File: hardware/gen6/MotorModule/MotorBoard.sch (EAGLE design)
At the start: 42 parts, among them J1 M20X2SHROUDED

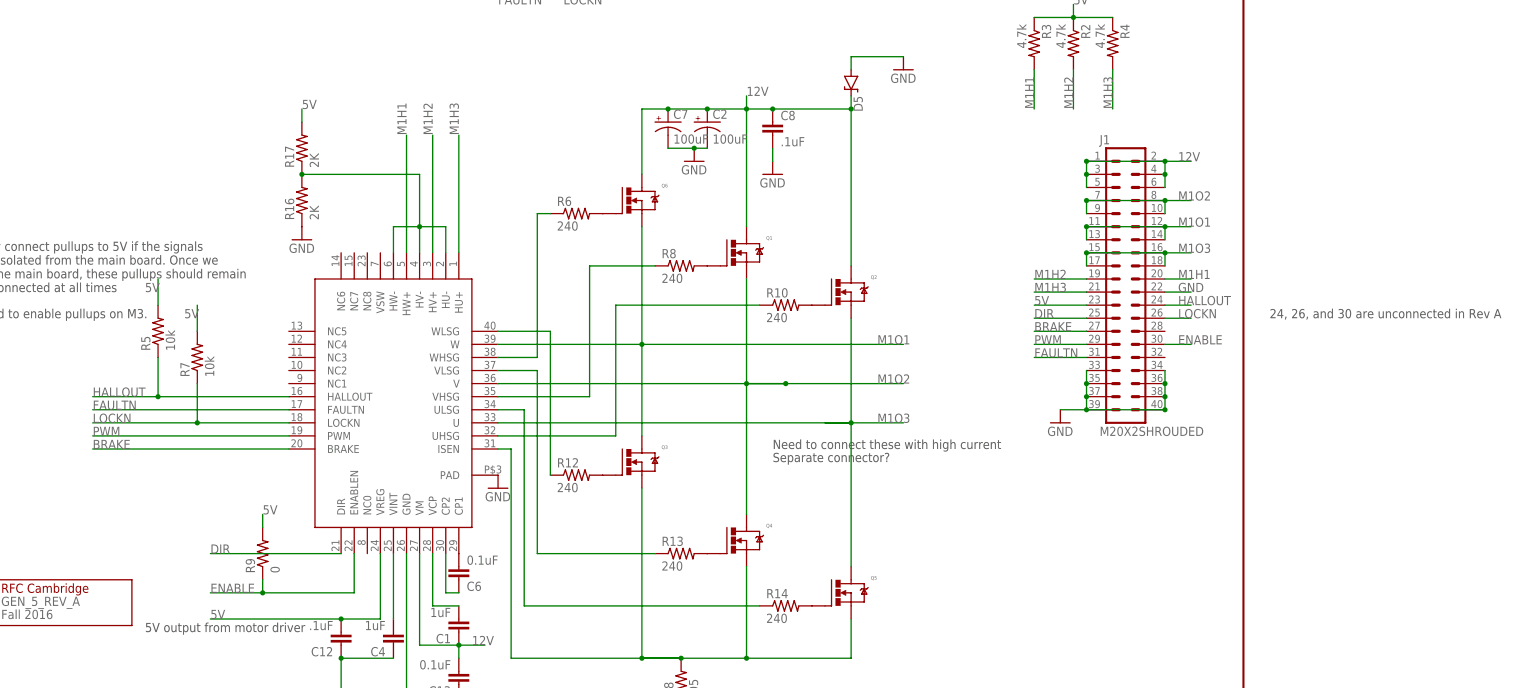
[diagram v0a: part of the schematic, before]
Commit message: new motor controller
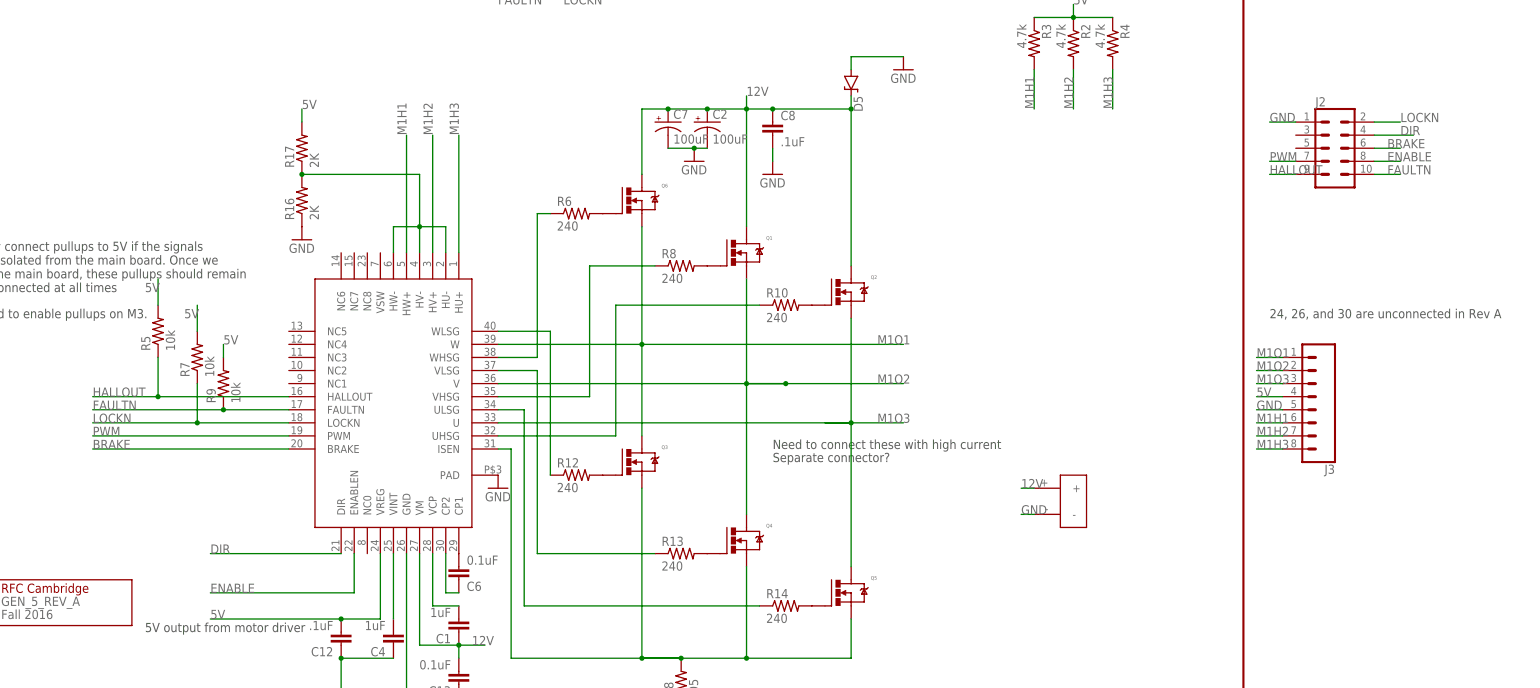
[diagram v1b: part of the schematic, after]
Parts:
- removed J1: M20X2SHROUDED, SparkFun-Connectors:M20X2SHROUDED
- added J2: (no value), SparkFun-Connectors:CONN_05X2SHD
- added J3: (no value), SparkFun-Connectors:CONN_08LONGPADS
- added U$2: POWER_CONN_2X1, Kicker:POWER_CONN_2X1
- R9: value 0 -> 10k
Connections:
- net 12V: now also U$2.+; no longer J1.1, J1.2, J1.3, J1.4, J1.5, J1.6
- net 5V: now also J3.4; no longer J1.23
- net BRAKE: now also J2.6; no longer J1.27
- net DIR: now also J2.4; no longer J1.25
- net ENABLE: now also J2.8; no longer J1.30, R9.1
- net FAULTN: now also J2.10, R9.1; no longer J1.31
- net GND: now also J2.1, J3.5, U$2.-; no longer J1.22, J1.33, J1.34, J1.35, J1.36, J1.37, J1.38, J1.39, J1.40
- net HALLOUT: now also J2.9; no longer J1.24
- net LOCKN: now also J2.2; no longer J1.26
- net M1H1: now also J3.6; no longer J1.20
- net M1H2: now also J3.7; no longer J1.19
- net M1H3: now also J3.8; no longer J1.21
- net M1O1: now also J3.1; no longer J1.11, J1.12, J1.13, J1.14
- net M1O2: now also J3.2; no longer J1.10, J1.7, J1.8, J1.9
- net M1O3: now also J3.3; no longer J1.15, J1.16, J1.17, J1.18
- net PWM: now also J2.7; no longer J1.29
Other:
- moved on the sheet: R9

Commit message: started conversion
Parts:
- added C3, C5: .1uF, SparkFun-Passives:CAP0805
- added IC1: 4011D, 40xx:4011D
- added R11, R25: 4.7k, SparkFun-Resistors:RESISTOR0805-RES
- added R15, R19, R20, R21, R22: 1k, SparkFun-Resistors:RESISTOR0805-RES
- added R23, R24: 10k, SparkFun-Resistors:RESISTOR0805-RES
- added U1: SN74LVC1G32DCKR, SparkFun-IC-Logic:74LVC32DBV
- added U2: 74HC1G04, SparkFun-IC-Logic:74HC1G04
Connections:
- new net N$12: R11.1, R15.1
- new net N$23: R19.2
- new net N$24: R19.1
- new net N$25: U1G1.A, U2G1.A
- new net N$26: IC1A.I1, U2G1.Y
- new net N$27: IC1A.I0, U1G1.B
- new net N$28: U1G1.Y
- new net N$29: R21.2
- new net N$30: R21.1
- new net N$31: IC1A.O
- new net N$32: R20.1
- new net N$33: R20.2
- new net N$34: R22.2, R23.1
- new net N$35: R23.2, R24.1
- new net N$36: R22.1, R24.2
- new net N$37: R25.2
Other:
- note added: "BRK"
- note added: "DIR"
- note added: "INa"
- note added: "INb"

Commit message: finished beginnings of schematic
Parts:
- added C10: 47uF, rcl:CPOL-US085CS-1AW
- added C9: .1uF, SparkFun-Passives:CAP0805
- added LED1, LED2: (no value), led:LED
- added Q7: IRFP250, transistor-power:IRFP250
- C3: value .1uF -> 33nF
- C5: value .1uF -> 47uF; device SparkFun-Passives:CAP0805 -> rcl:CPOL-US085CS-1AW
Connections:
- removed net N$33: R20.2
- new net +5V: Q7.S
- new net N$38: LED1.C, LED2.A, R25.1
- new net N$39: LED1.A, LED2.C
- net GND: now also C10.-, C3.2, C5.-, C9.1, R22.1, R24.2
- net N$35: now also C3.1, R20.2
- net N$36: now also C10.+, C5.+, C9.2, Q7.D; no longer R22.1, R24.2
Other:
- note added: "JP7"
- note added: "check with schematic"

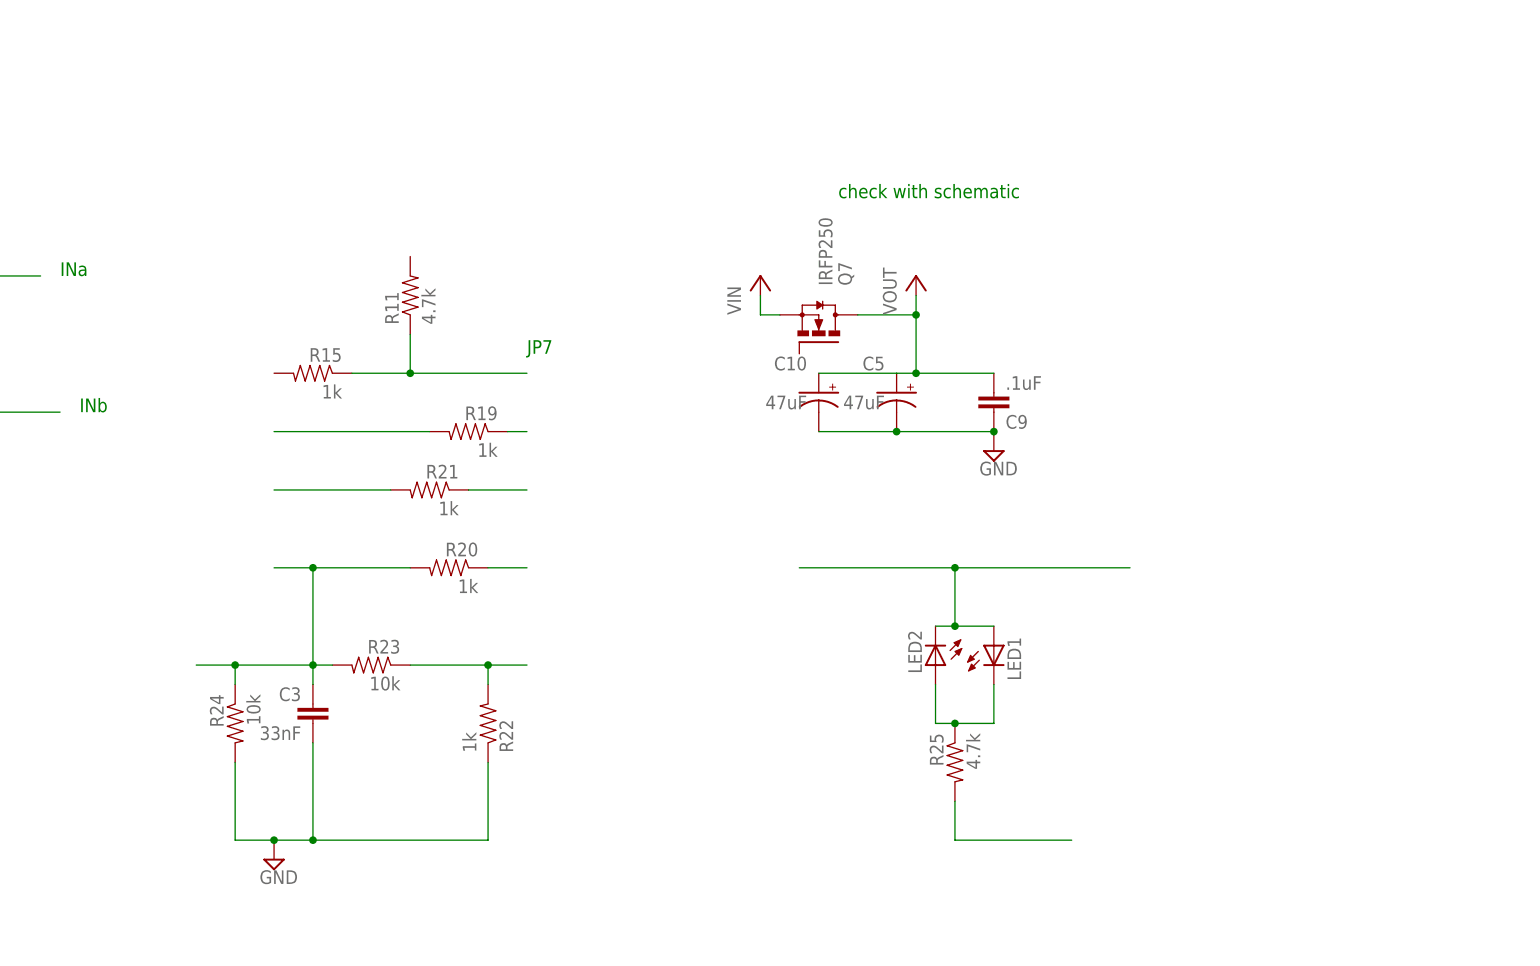
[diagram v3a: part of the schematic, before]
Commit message: added VNH5019A-E package to schematic
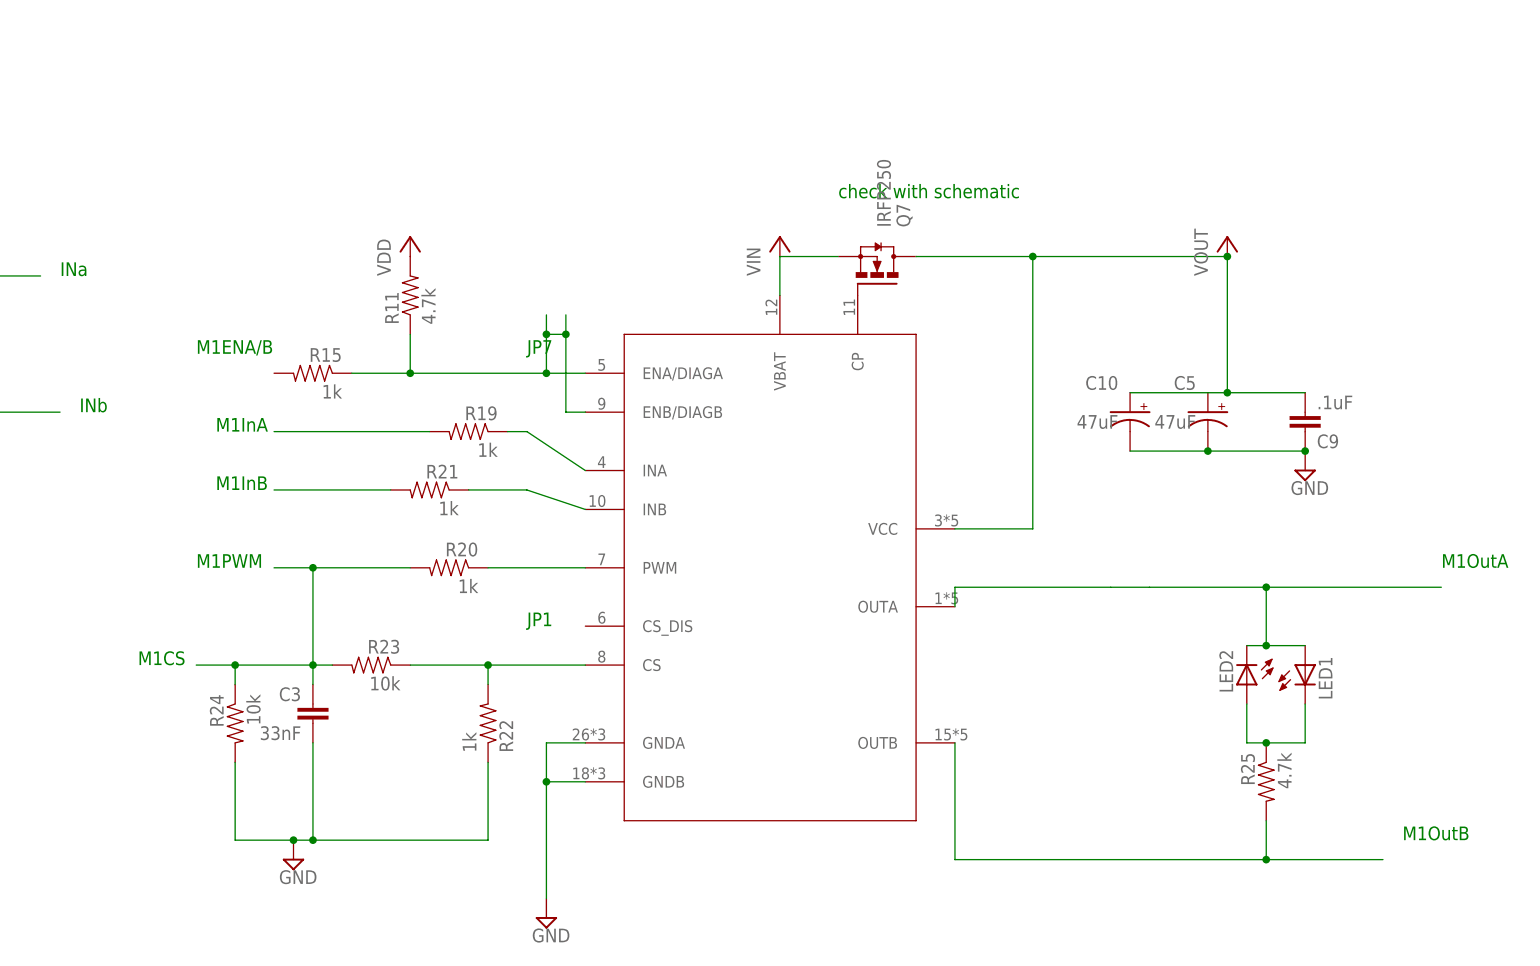
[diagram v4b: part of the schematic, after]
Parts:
- added U$3: VNH5019A-E, st-microelectronics:VNH5019A-E
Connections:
- new net N$3: Q7.G, U$3.CP
- net +5V: now also R11.2, U$3.VBAT
- net GND: now also U$3.GNDA, U$3.GNDB
- net N$12: now also U$3.ENA/DIAGA, U$3.ENB/DIAGB
- net N$24: now also U$3.INA
- net N$30: now also U$3.INB
- net N$32: now also U$3.PWM
- net N$34: now also U$3.CS
- net N$36: now also U$3.VCC
- net N$37: now also U$3.OUTB
- net N$39: now also U$3.OUTA
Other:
- note added: "JP1"
- note added: "M1CS"
- note added: "M1ENA/B"
- note added: "M1InA"
- note added: "M1InB"
- note added: "M1OutA"
- note added: "M1OutB"
- note added: "M1PWM"
- moved on the sheet: C10, C5, C9, LED1, LED2, Q7, R25

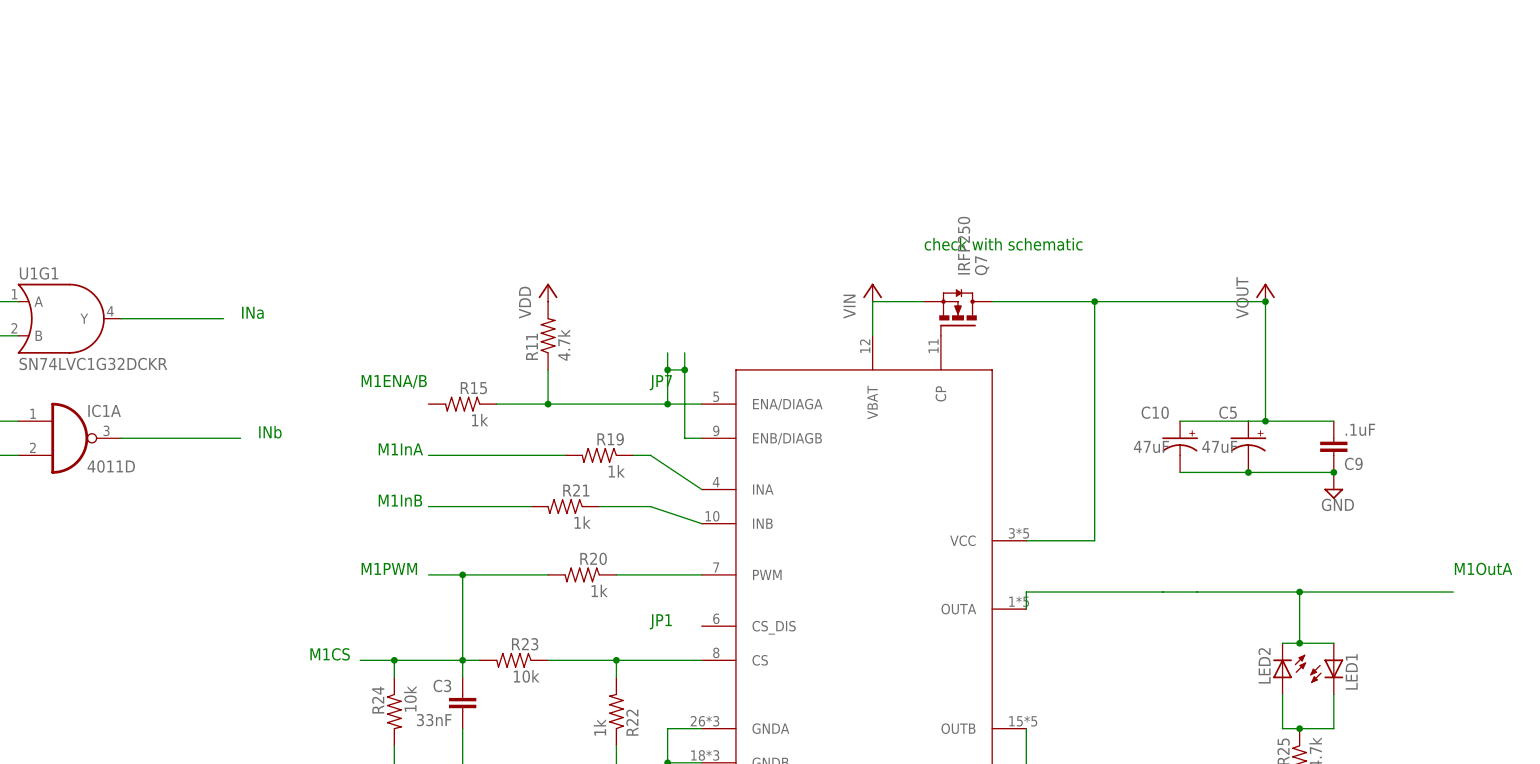
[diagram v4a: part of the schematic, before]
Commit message: dealt with J7, J1, and Q1
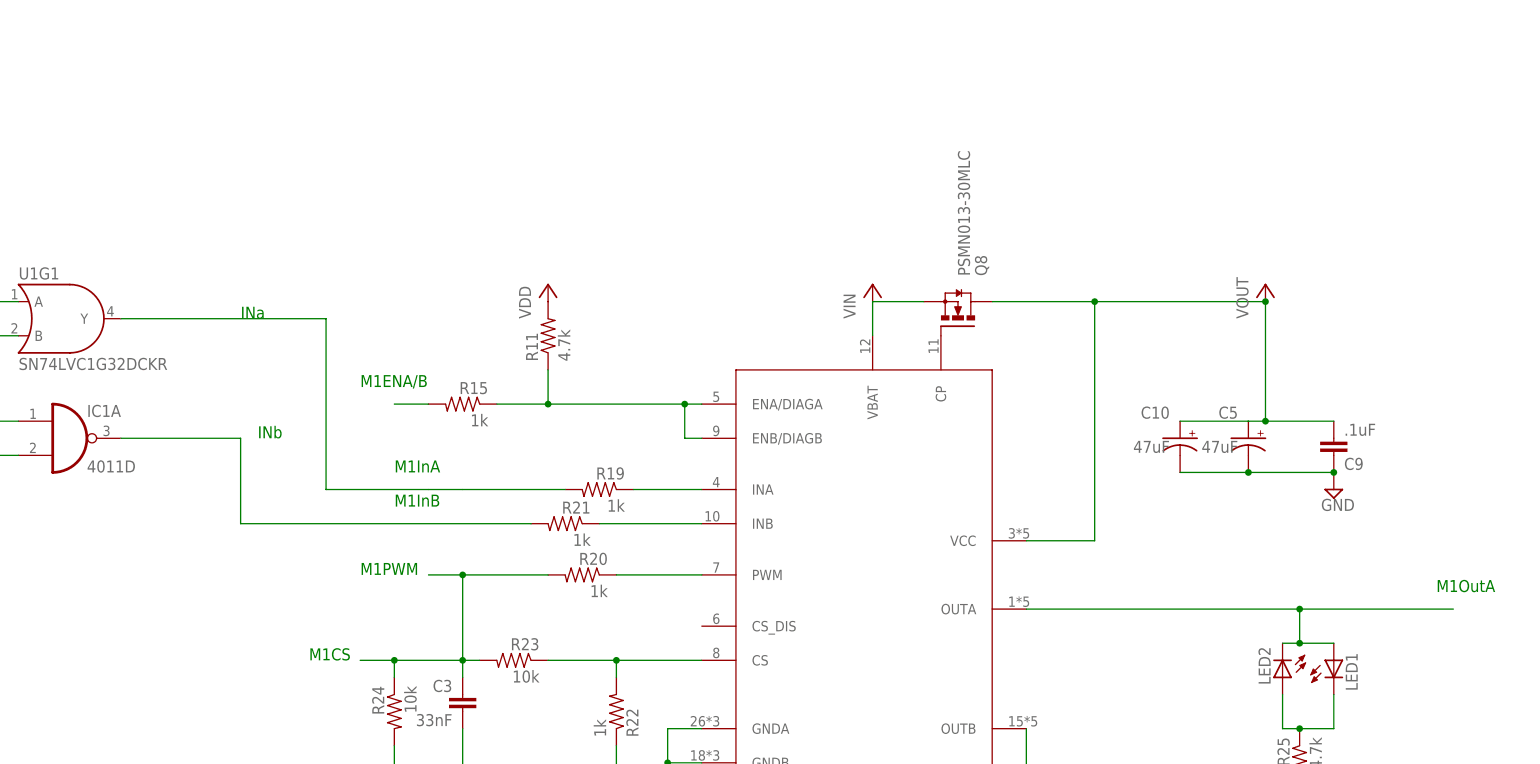
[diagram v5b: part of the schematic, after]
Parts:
- removed Q7: IRFP250, transistor-power:IRFP250
- added Q8: PSMN013-30MLC, transistor-power:PSMN013-30MLC
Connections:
- removed net N$31: IC1A.O
- removed net N$5: R19.2
- new net N$8: R15.2
- net +5V: now also Q8.S; no longer Q7.S
- net N$28: now also R19.2
- net N$29: now also IC1A.O
- net N$3: now also Q8.G; no longer Q7.G
- net N$36: now also Q8.D; no longer Q7.D
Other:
- note removed: "JP1"
- note removed: "JP7"
- note removed: "check with schematic"
- moved on the sheet: R19, R21

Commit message: safety commit
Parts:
- removed J2: (no value), SparkFun-Connectors:CONN_05X2SHD
- removed J3: (no value), SparkFun-Connectors:CONN_08LONGPADS
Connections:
- net N$35 renamed CS
- net N$37 renamed M1OUTB
- net N$39 renamed M1OUTA
- removed net N$25: U1G1.A, U2G1.A
- removed net N$27: IC1A.I0, U1G1.B
- removed net N$8: R15.2
- new net 0: U$3.GNDA, U$3.GNDB
- net 5V: no longer J3.4
- net BRAKE: now also U1G1.A, U2G1.A; no longer J2.6
- net DIR: now also IC1A.I0, U1G1.B; no longer J2.4
- net ENABLE: now also R15.2; no longer J2.8
- net FAULTN: no longer J2.10
- net GND: no longer J2.1, J3.5, U$3.GNDA, U$3.GNDB
- net HALLOUT: no longer J2.9
- net LOCKN: no longer J2.2
- net M1H1: no longer J3.6
- net M1H2: no longer J3.7
- net M1H3: no longer J3.8
- net M1O1: no longer J3.1
- net M1O2: no longer J3.2
- net M1O3: no longer J3.3
- net PWM: no longer J2.7
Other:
- note removed: "24, 26, and 30 are unconnected in Rev A"
- note removed: "BRK"
- note removed: "DIR"
- note removed: "M1CS"
- note removed: "M1ENA/B"
- note removed: "M1OutA"
- note removed: "M1OutB"
- note removed: "M1PWM"
